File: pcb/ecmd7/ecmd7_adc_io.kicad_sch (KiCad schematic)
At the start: 71 parts, among them U10 FIN1002M5X, U11 FIN1002M5X, U12 FIN1002M5X, U13 ADM3490ExR, U2 MCP33151-05T-E/MN, U4 MCP33151-05T-E/MN, U5 MCP33151-05T-E/MN, U7 MCP33151-05T-E/MN

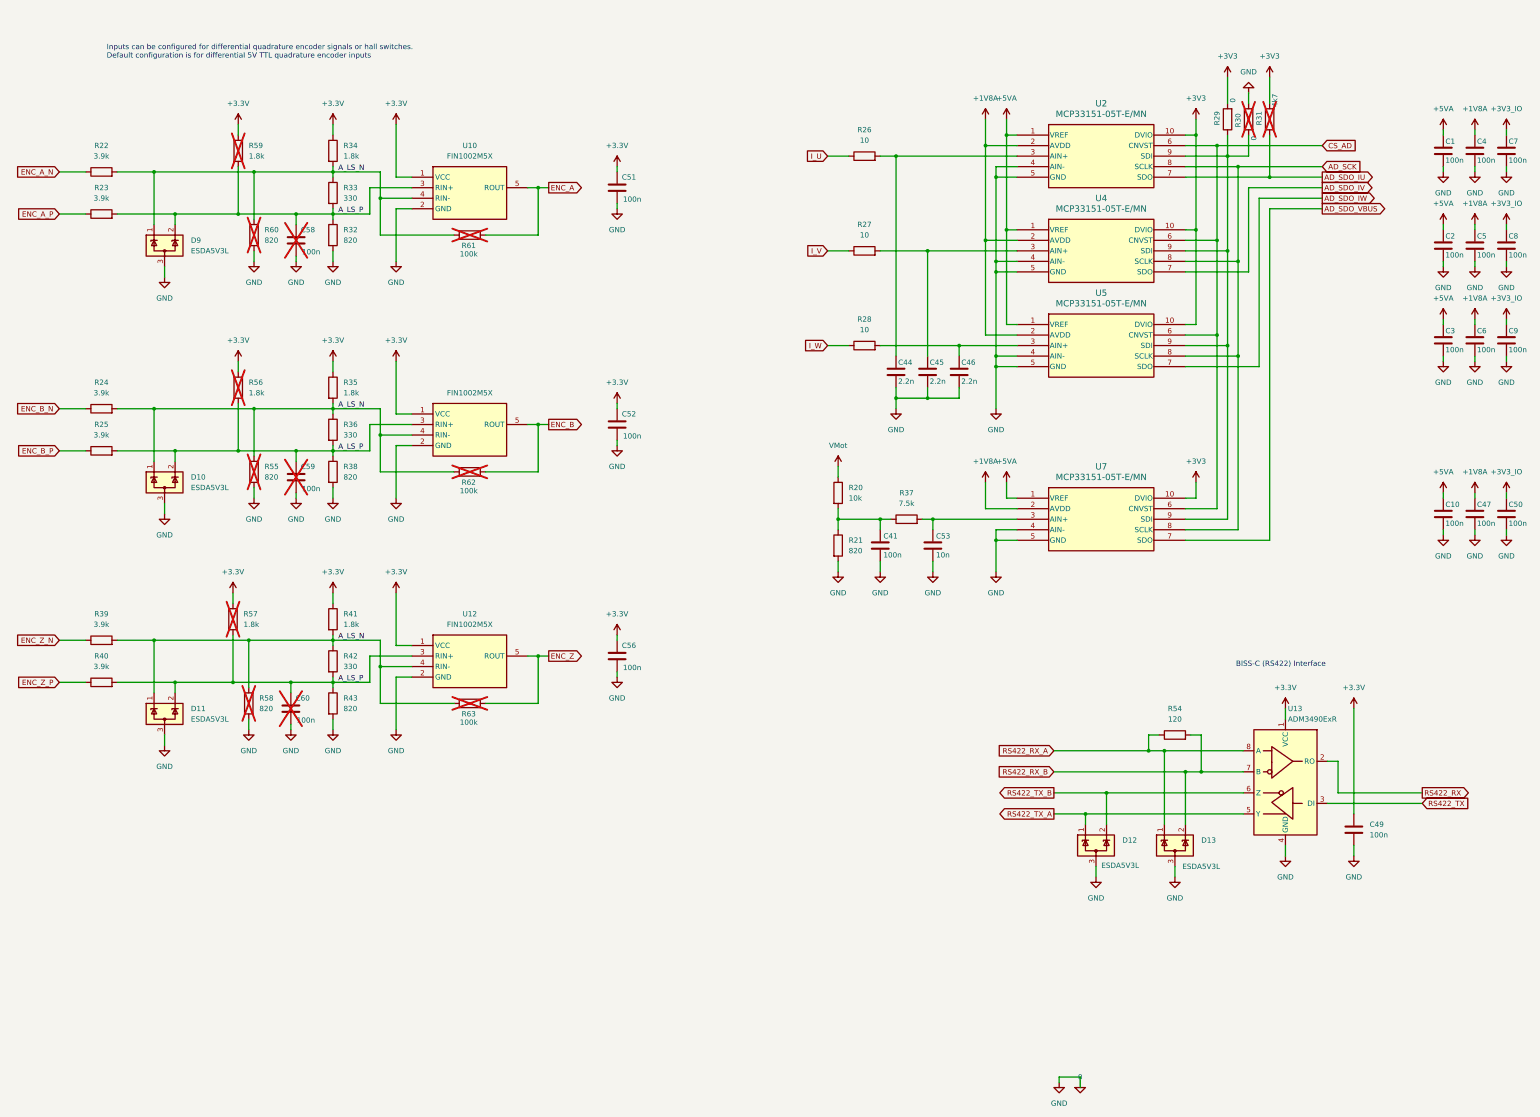
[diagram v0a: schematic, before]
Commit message: Initial component placement
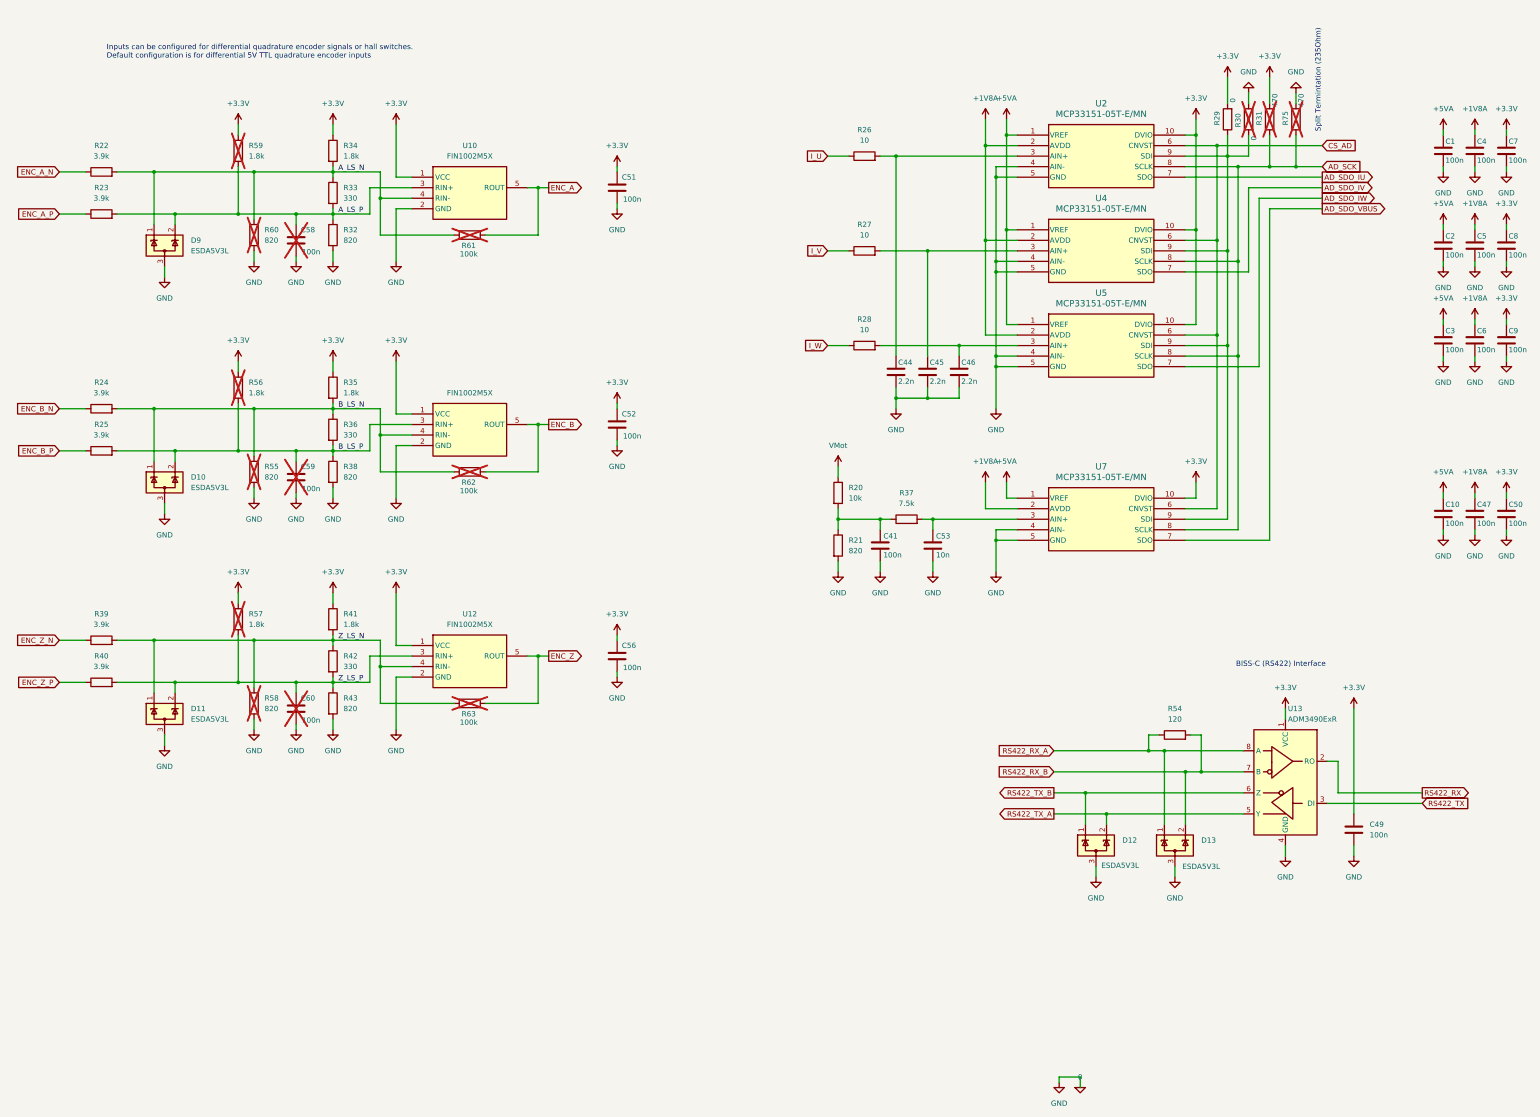
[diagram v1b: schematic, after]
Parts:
- added R75: 470, Resistor_SMD:R_0805_2012Metric, symbol Device:R
- R31: value 4k7 -> 470
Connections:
- net +3V3 is gone; now on net +3.3V: R29.2, R31.2, U2.10 (DVIO), U4.10 (DVIO), U5.10 (DVIO), U7.10 (DVIO)
- net +3V3_IO is gone; now on net +3.3V: C50.1, C7.1, C8.1, C9.1
- net 0: now also R75.2
- net AD_SCK: now also R31.1, R75.1
- net AD_SDO_IU: no longer R31.1
- net A_LS_N: no longer D10.1 (K), D11.1 (K), R24.2, R35.2, R36.1, R39.2, R41.2, R42.1, R55.1, R58.1, R62.1, R63.1, U11.4 (RIN-), U12.4 (RIN-)
- net A_LS_P: no longer C59.1, C60.1, D10.2 (K), D11.2 (K), R25.2, R36.2, R38.1, R40.2, R42.2, R43.1, R56.2, R57.2, U11.3 (RIN+), U12.3 (RIN+)
- net RS422_TX_A: now also D12.2 (K); no longer D12.1 (K)
- net RS422_TX_B: now also D12.1 (K); no longer D12.2 (K)
- new net B_LS_N: D10.1 (K), R24.2, R35.2, R36.1, R55.1, R62.1, U11.4 (RIN-)
- new net B_LS_P: C59.1, D10.2 (K), R25.2, R36.2, R38.1, R56.2, U11.3 (RIN+)
- new net Z_LS_N: D11.1 (K), R39.2, R41.2, R42.1, R58.1, R63.1, U12.4 (RIN-)
- new net Z_LS_P: C60.1, D11.2 (K), R40.2, R42.2, R43.1, R57.2, U12.3 (RIN+)
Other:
- note added: "Split Termintation (235Ohm)"
- moved on the sheet: C60, R57, R58

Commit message: WIP: Update symbols, fix ERC errors
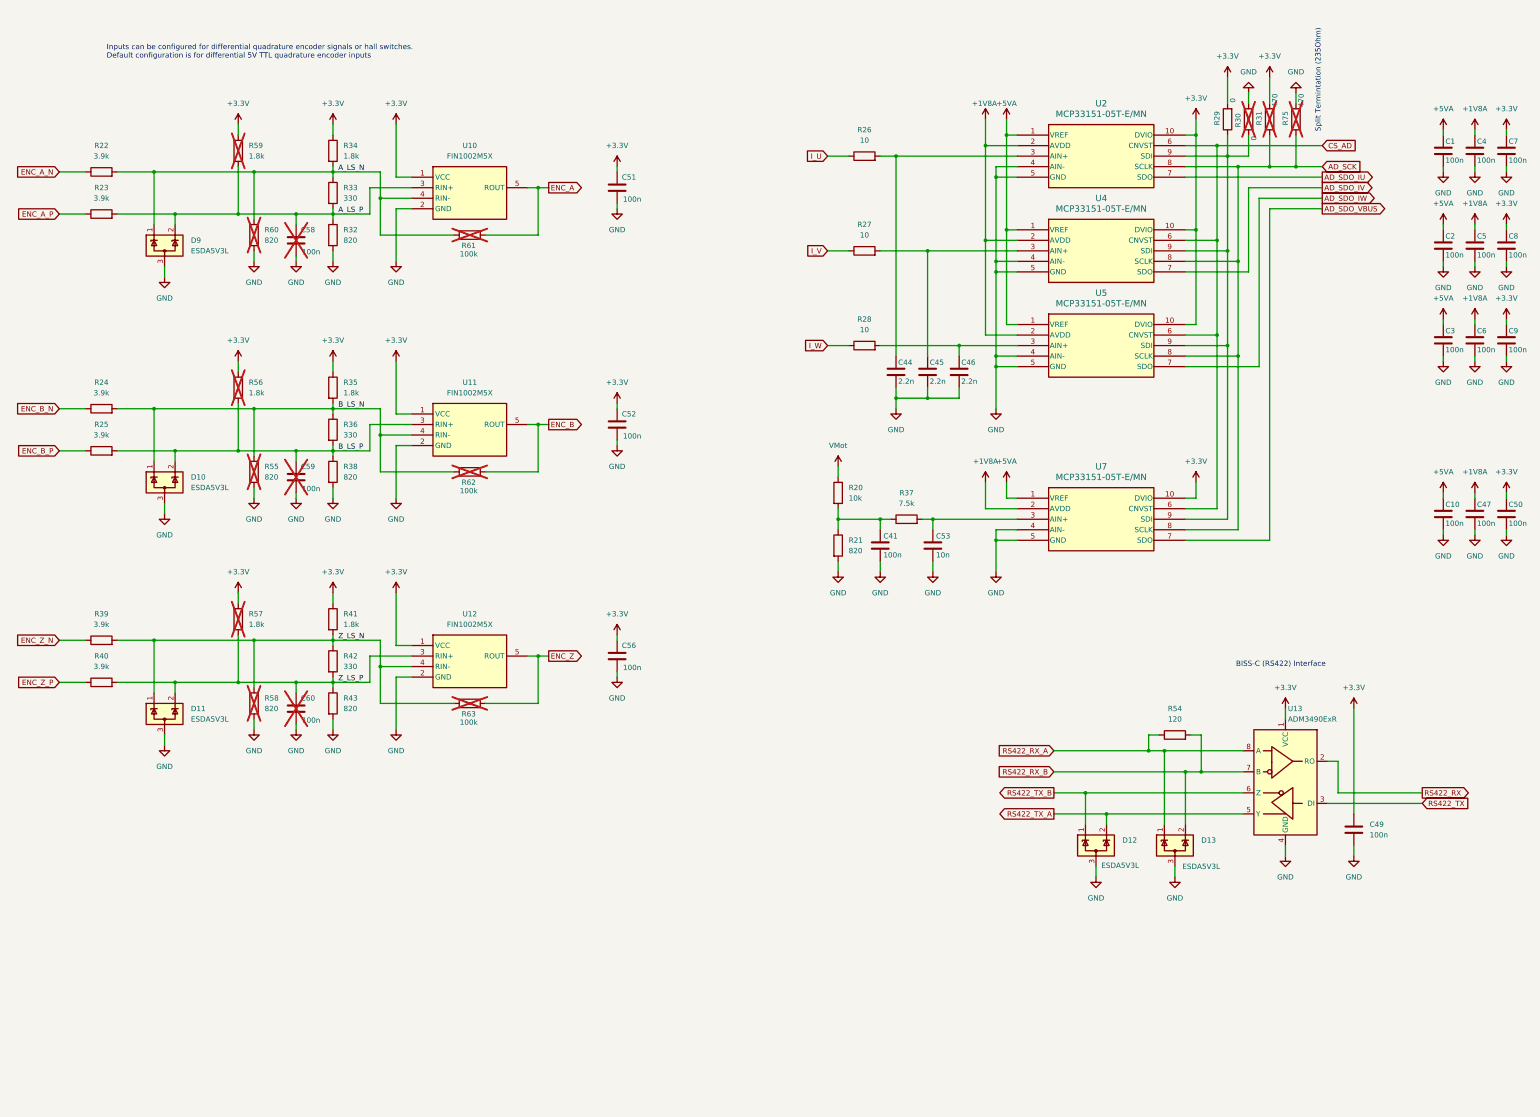
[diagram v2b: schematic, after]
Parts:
- U10, U11, U12: symbol ssta_symbols:FIN1002M5X -> SSTA:FIN1002M5X
- U2, U4, U5, U7: footprint sst_footprints:TDFN10_MN_MCH -> SSTA:TDFN10_MN_MCH; symbol ssta_symbols:MCP33151-05T-E_MN -> SSTA:MCP33151-05T-E_MN
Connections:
- net 0 renamed GND

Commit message: WIP: Power stage and ADC routing
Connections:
- net GND: no longer C41.2, C44.2, C45.2, C46.2, C53.2, R21.2, U2.4 (AIN-), U4.4 (AIN-), U5.4 (AIN-), U7.4 (AIN-)
- new net I_REF: C44.2, C45.2, C46.2, U2.4 (AIN-), U4.4 (AIN-), U5.4 (AIN-)
- new net VMOT_REF: C41.2, C53.2, R21.2, U7.4 (AIN-)
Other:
- moved on the sheet: R20

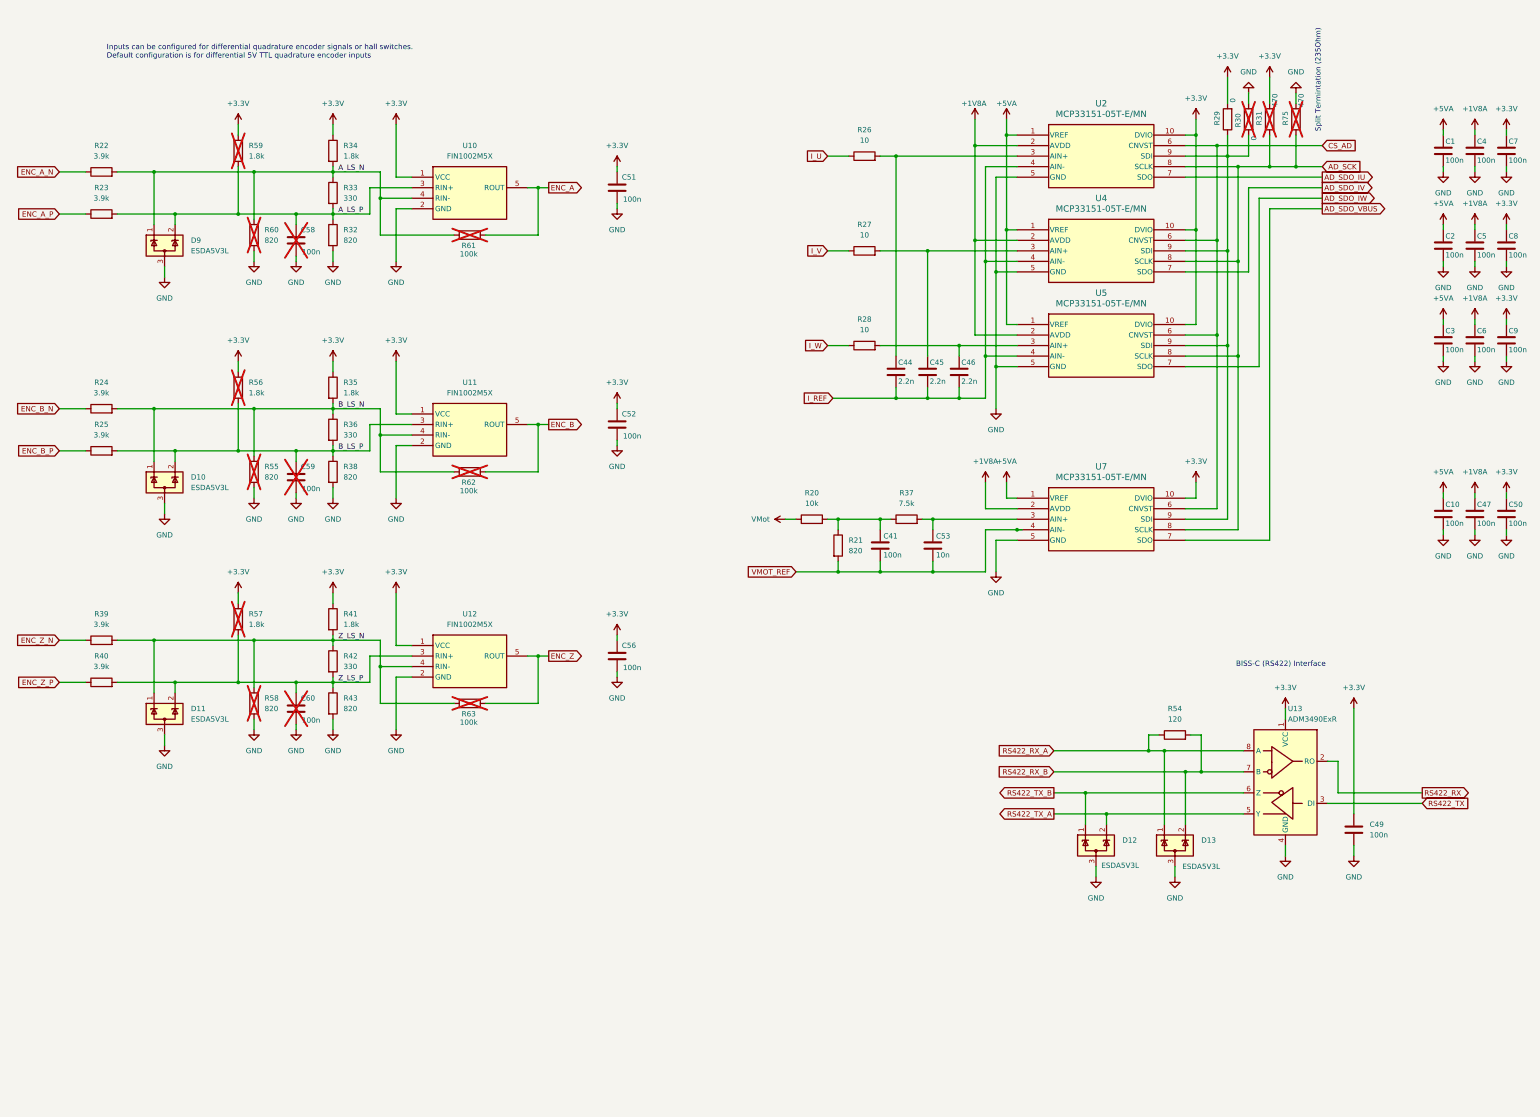
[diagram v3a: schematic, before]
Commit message: WIP: Partial routing
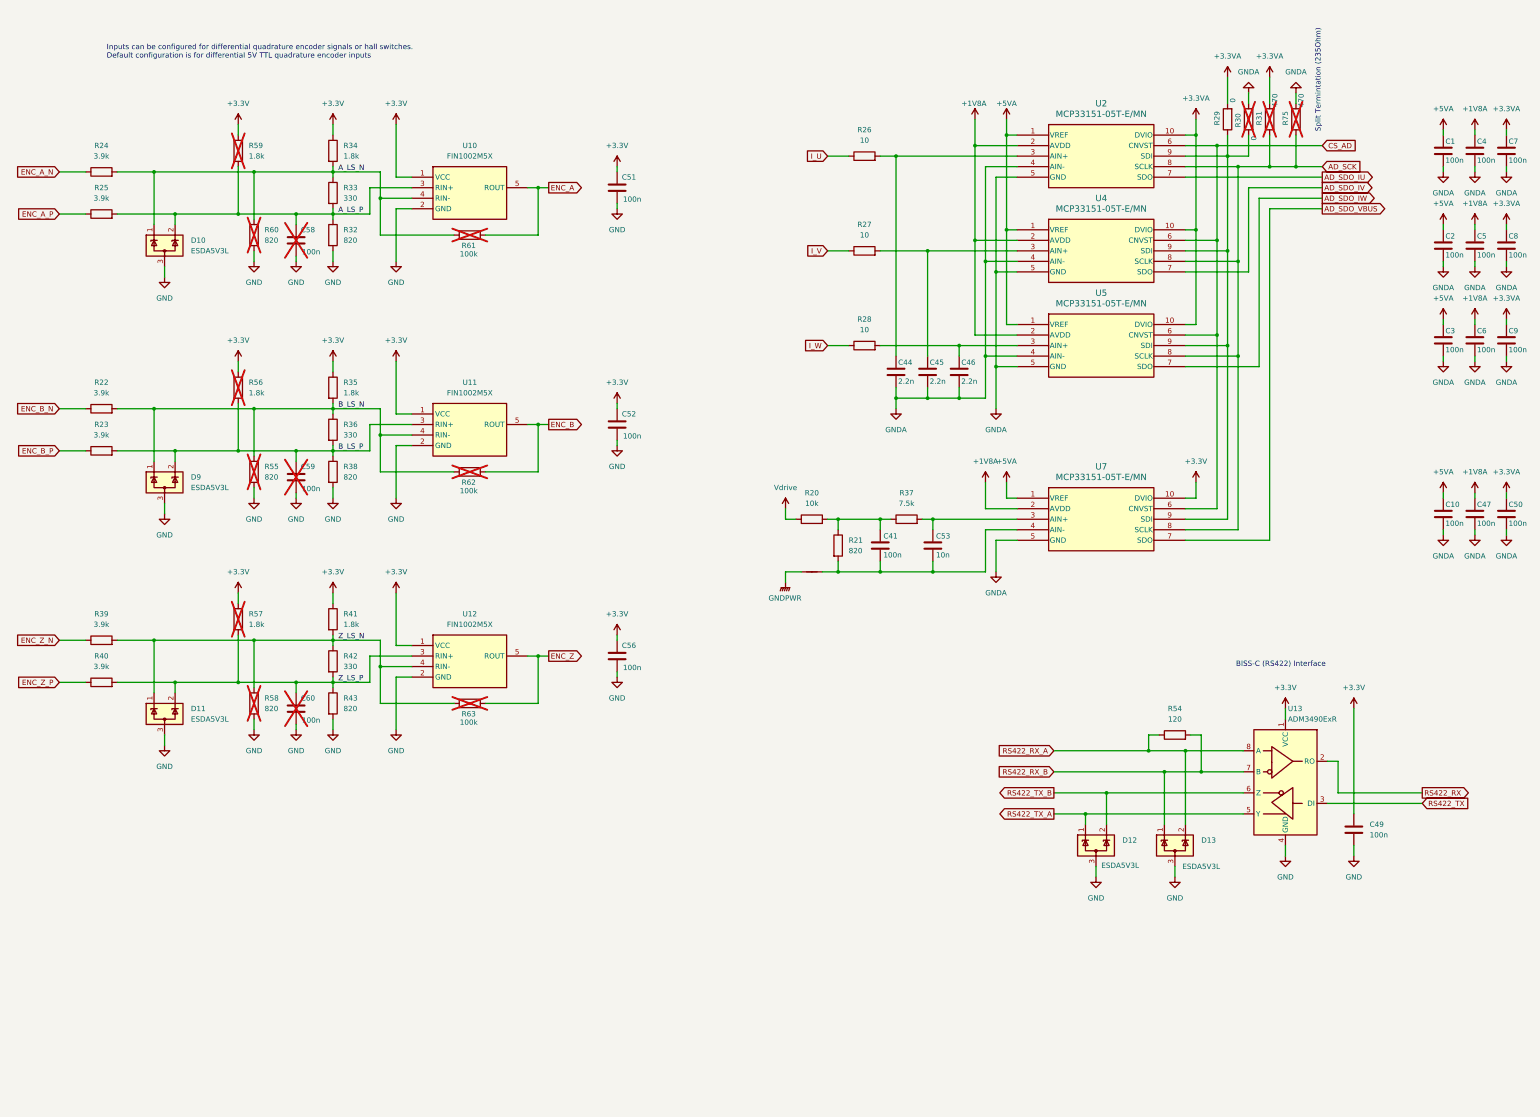
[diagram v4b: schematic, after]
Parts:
- added NTP2G3: NetTie_2, NetTie:NetTie-2_SMD_Pad0.5mm, symbol Device:NetTie_2
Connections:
- net +3.3V: no longer C50.1, C7.1, C8.1, C9.1, R29.2, R31.2, U2.10 (DVIO), U4.10 (DVIO), U5.10 (DVIO)
- net A_LS_N: now also D10.1 (K), R24.2; no longer D9.1 (K), R22.2
- net A_LS_P: now also D10.2 (K), R25.2; no longer D9.2 (K), R23.2
- net B_LS_N: now also D9.1 (K), R22.2; no longer D10.1 (K), R24.2
- net B_LS_P: now also D9.2 (K), R23.2; no longer D10.2 (K), R25.2
- net ENC_A_N: now also R24.1; no longer R22.1
- net ENC_A_P: now also R25.1; no longer R23.1
- net ENC_B_N: now also R22.1; no longer R24.1
- net ENC_B_P: now also R23.1; no longer R25.1
- net GND: no longer C1.2, C10.2, C2.2, C3.2, C4.2, C47.2, C5.2, C50.2, C6.2, C7.2, C8.2, C9.2, R30.1, R75.2, U2.5 (GND), U4.5 (GND), U5.5 (GND), U7.5 (GND)
- net RS422_RX_A: now also D13.2 (K); no longer D13.1 (K)
- net RS422_RX_B: now also D13.1 (K); no longer D13.2 (K)
- net RS422_TX_A: now also D12.1 (K); no longer D12.2 (K)
- net RS422_TX_B: now also D12.2 (K); no longer D12.1 (K)
- net I_REF renamed GNDA
- net GNDA: now also C1.2, C10.2, C2.2, C3.2, C4.2, C47.2, C5.2, C50.2, C6.2, C7.2, C8.2, C9.2, R30.1, R75.2, U2.5 (GND), U4.5 (GND), U5.5 (GND), U7.5 (GND)
- net VMOT_REF: no longer names the net of C41.2, C53.2, R21.2, U7.4 (AIN-)
- net VMOT_REF: now also NTP2G3.1
- net VMot renamed Vdrive
- new net +3.3VA: C50.1, C7.1, C8.1, C9.1, R29.2, R31.2, U2.10 (DVIO), U4.10 (DVIO), U5.10 (DVIO)
- new net GNDPWR: NTP2G3.2
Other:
- moved on the sheet: D10, D9, R22, R23, R24, R25
